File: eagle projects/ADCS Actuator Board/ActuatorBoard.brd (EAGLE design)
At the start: 91 x 91 mm, 278 parts, among them J19 TE_1-84953-1, J20 TE_1-84953-1, J21 TE_1-84953-1, U10 DRV10970_MOTOR_DRIVERDRV10970, U12 DRV10970_MOTOR_DRIVERDRV10970, U13 ADS7841E_2K5, U15 TLV9051IDCKR, U19 TLV9051IDCKR, U2 ADS7841E_2K5, U21 TLV9051IDCKR, U23 TLV9051IDCKR, U24 TLV9051IDCKR, U25 ADS7841E_2K5, U26 TLV9051IDCKR, U27 ADS7841E_2K5, U28 TLV9051IDCKR, U29 TLV9051IDCKR, U3 ADS7841E_2K5, U30 TLV9051IDCKR, U31 TLV9051IDCKR, U32 TLV9051IDCKR, U34 TVS991, U35 BD6210F-E2, U38 TVS991, U39 BD6210F-E2, U4 ADS7841E_2K5, U5 TVS991, U6 TLV9051IDCKR, U7 DRV10970_MOTOR_DRIVERDRV10970, U9 BD6210F-E2

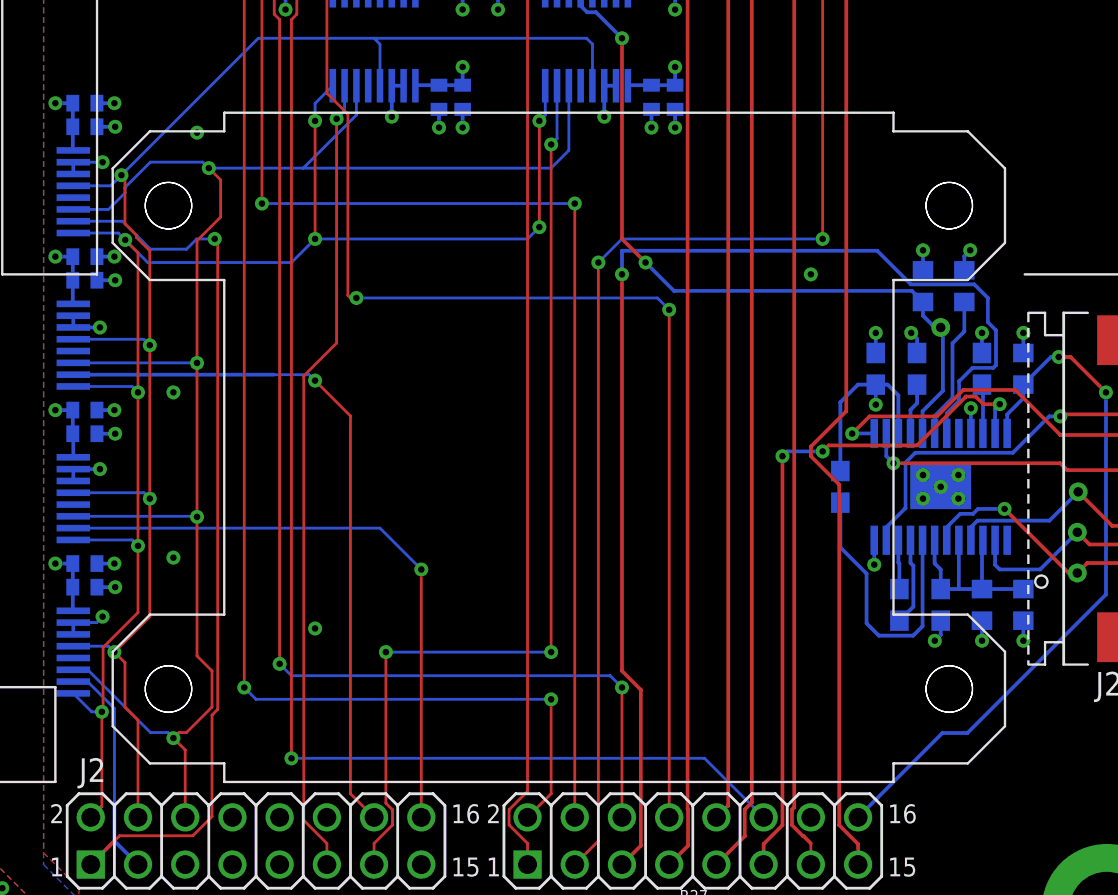
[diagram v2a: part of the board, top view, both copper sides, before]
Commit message: Updated new reaction wheel footprint, silk and 3d model
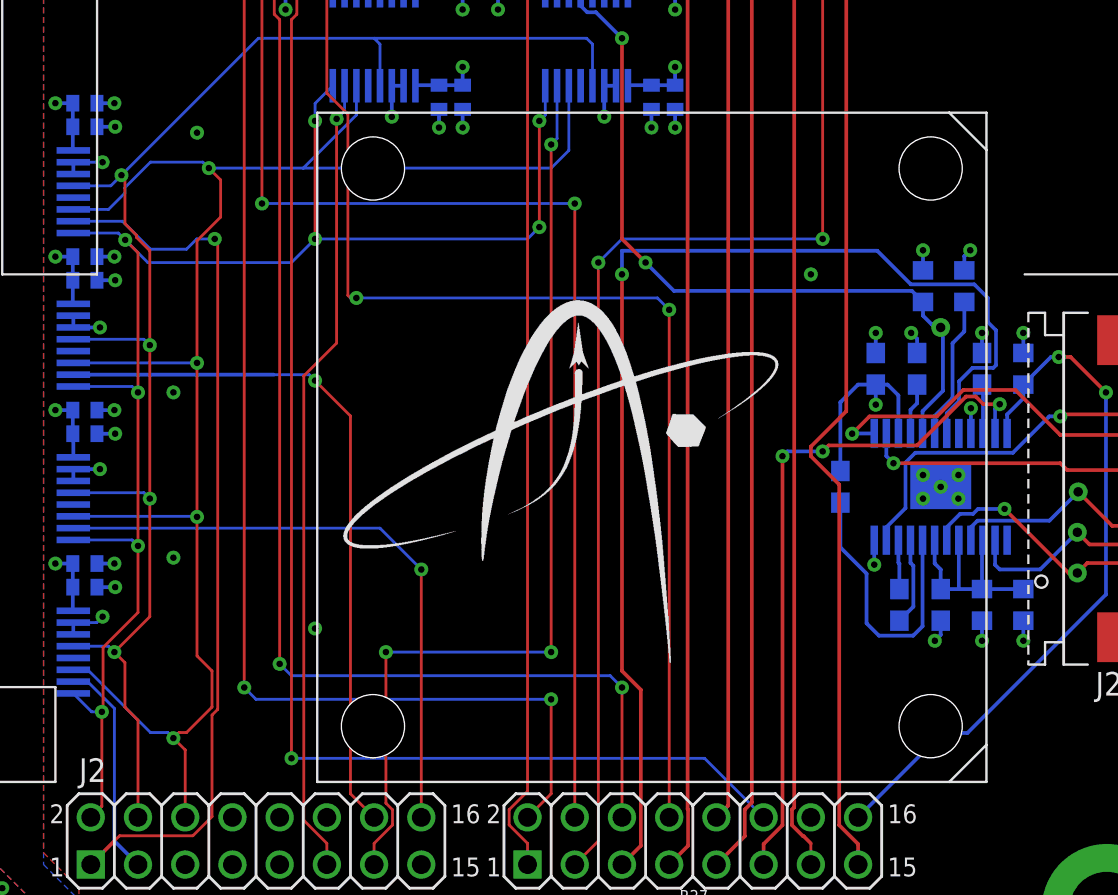
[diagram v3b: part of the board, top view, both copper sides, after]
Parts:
- moved RWZ 5.00 mm to (78.0, 13.3)

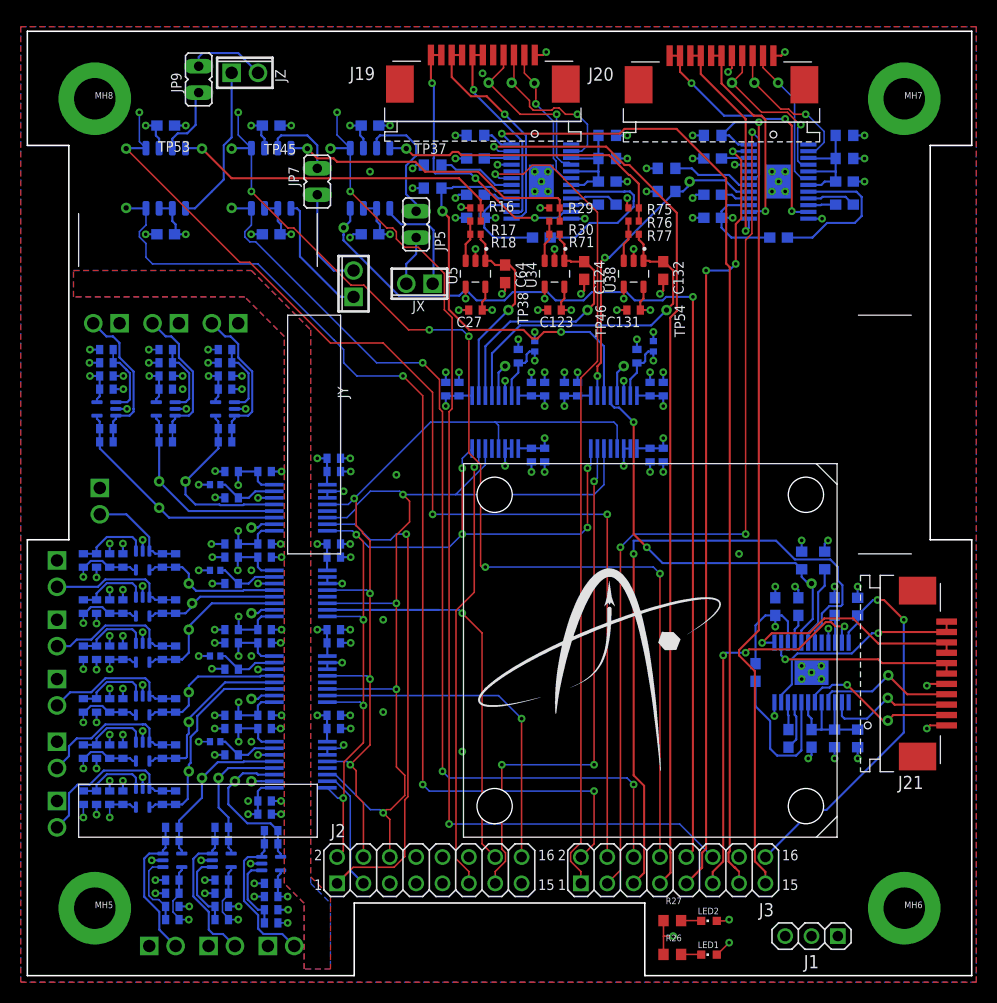
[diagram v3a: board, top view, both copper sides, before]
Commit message: Updates to layout silk/traces
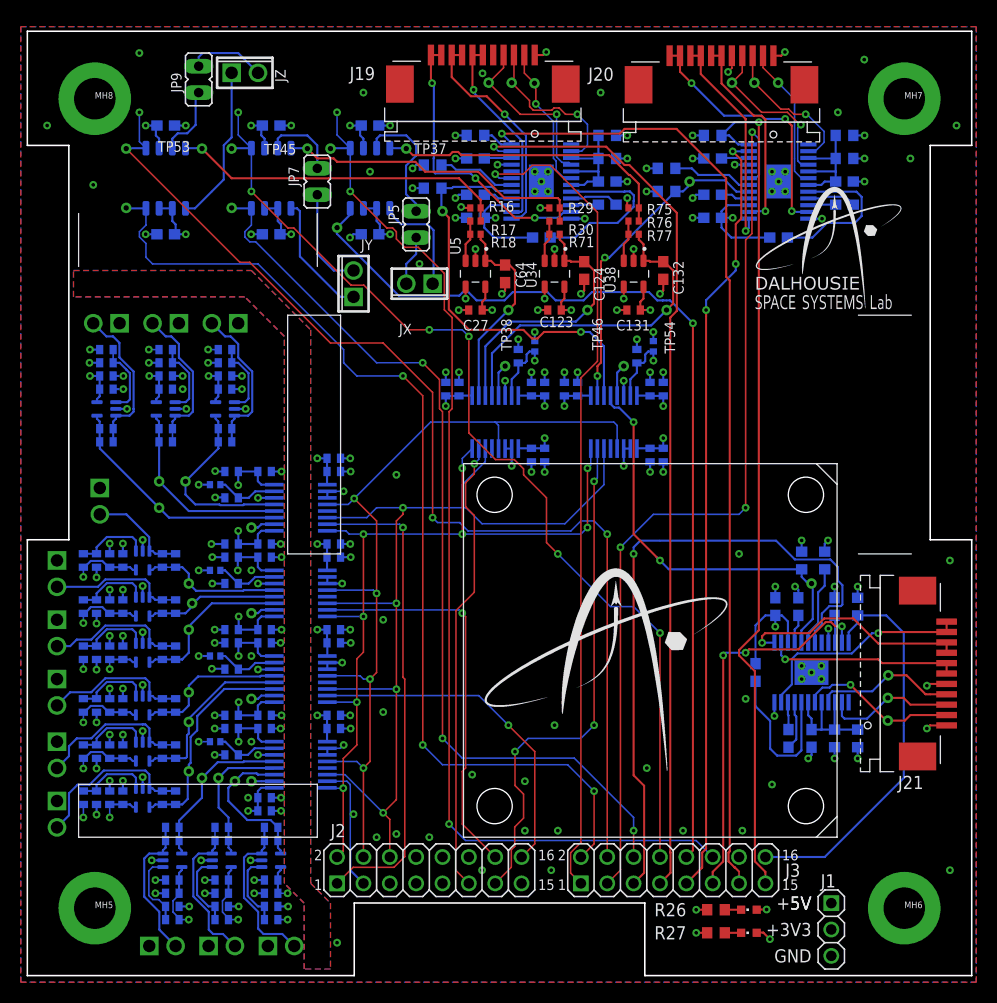
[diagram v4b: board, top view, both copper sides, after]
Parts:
- moved R26 6.02 mm to (66.4, 6.35)
- moved LED1 5.79 mm to (69.5, 6.35)
- moved R27 4.37 mm to (66.4, 4.13)
- moved LED2 4.01 mm to (69.5, 4.13)
- moved J1 2.01 mm to (77.5, 4.45), turned to 270 degrees
- moved TP35 0.64 mm to (29.8, 72.1)
- moved C91 0.32 mm to (22.9, 15.9)
- moved R62 0.32 mm to (23.5, 6.67)
- moved R64 0.32 mm to (23.5, 13.0)
- moved U30 0.32 mm to (23.5, 11.1)
- moved C96 0.32 mm to (23.5, 7.94)
- moved R63 0.32 mm to (23.5, 5.40)
- moved C92 0.32 mm to (22.9, 17.1)
- moved C97 0.32 mm to (23.5, 9.21)
- moved C98 0.32 mm to (23.5, 14.3)
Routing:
- net MAG_Y_RIN: track 104.3 -> 97.0 mm
- net MAG_Y_FIN: track 93.2 -> 89.5 mm
- net UCB0_SPI_CLK: track 84.5 -> 81.9 mm
- net MAG_Z_FIN: track 101.2 -> 99.0 mm
- net GND: track 170.7 -> 168.6 mm, vias 176 -> 177
- net !CS!_CUR_SENSE_RW: track 51.5 -> 49.6 mm
- net UCB0_SPI_MISO: track 83.6 -> 85.1 mm
- net RW_Y_SPEED_CTRL: track 90.0 -> 88.5 mm
- net RW_Y_DIR: track 75.9 -> 74.6 mm
- net MAG_X_FIN: track 95.4 -> 94.2 mm
- net RW_Z_I_SENS: track 40.3 -> 41.2 mm
- net UCB0_SPI_MOSI: track 95.1 -> 94.3 mm
- net +5V: track 66.4 -> 65.7 mm
- net !CS!_CUR_SENSE_MAG: track 43.3 -> 44.0 mm
- net !CS!_SUN_Y+: track 11.7 -> 12.4 mm
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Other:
- board text added: "+3V3"
- board text added: "+5V"
- board text added: "5V"
- board text added: "GND"

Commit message: Slight layout tweaks
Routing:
- net RW_Y_SPEED_CTRL: track 88.5 -> 82.5 mm
- net RW_Y_OUTFG: track 82.3 -> 77.4 mm
- net UCB0_SPI_CLK: track 81.9 -> 77.0 mm, vias 8 -> 7
- net Z_PHASE_B: track 22.4 -> 20.0 mm
- net MAG_Z_FIN: track 99.0 -> 101.2 mm
- net RW_Z_DIR: track 36.9 -> 38.0 mm
- net MAG_Z_RIN: track 106.4 -> 107.3 mm
- net Y_PHASE_B: track 21.0 -> 20.4 mm
- net !CS!_CUR_SENSE_RW: track 49.6 -> 49.1 mm

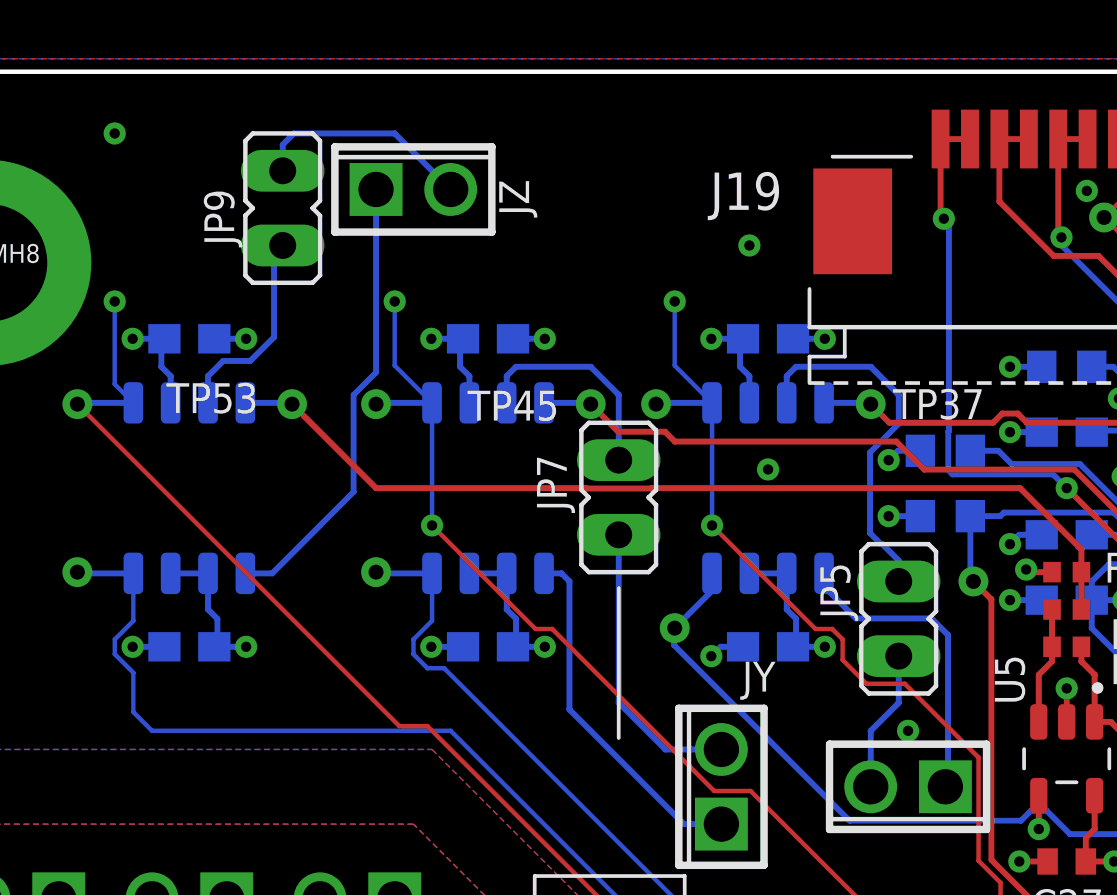
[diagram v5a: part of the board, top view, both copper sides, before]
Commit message: Replaced jumpers with circular pads
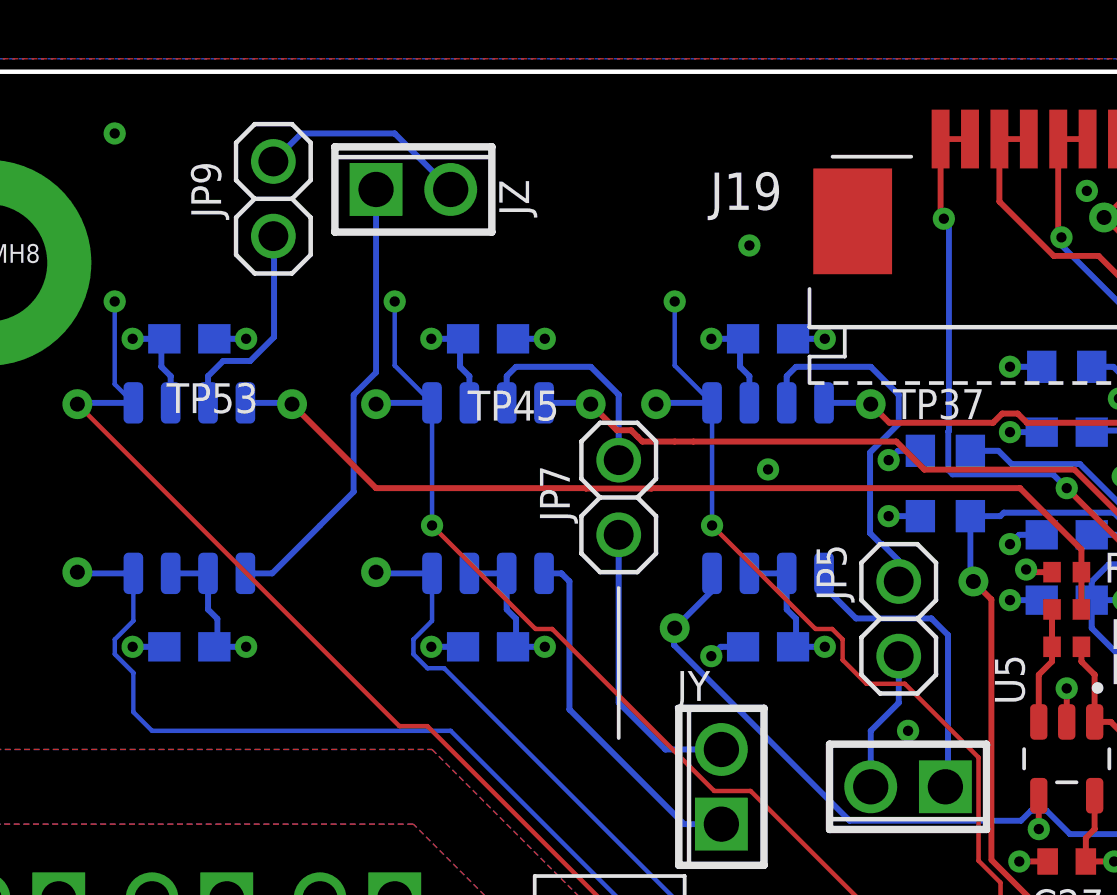
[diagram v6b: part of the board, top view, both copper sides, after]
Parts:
- JP5, JP7, JP9: device jumper:JP1 -> my_library:1X02
- moved JP9 0.45 mm to (16.2, 86.7), turned to 270 degrees
- turned JP5 to 90 degrees
- turned JP7 to 90 degrees
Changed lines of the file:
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@@
 <attribute name="SPICEPREFIX" value="C" x="33.02" y="61.9125" size="1.778" layer="28" rot="MR180" display="off"/>
 </element>
-<element name="JP5" library="jumper" library_urn="urn:adsk.eagle:library:252" package="JP1" package3d_urn="urn:adsk.eagle:package:15455/1" value="" x="37.465" y="72.39" smashed="yes">
-<attribute name="NAME" x="35.814" y="72.39" size="1.016" layer="25" ratio="10" rot="R90"/>
-<attribute name="POPULARITY" value="15" x="29.845" y="76.835" size="1.778" layer="27" display="off"/>
-<attribute name="VALUE" x="40.386" y="69.85" size="1.27" layer="27" ratio="10" rot="R90"/>
+<element name="JP5" library="my_library" library_urn="urn:adsk.eagle:library:22876504" package="1X02" package3d_urn="urn:adsk.eagle:package:24527019/1" value="" x="37.465" y="72.39" smashed="yes" rot="R90">
+<attribute name="NAME" x="34.671" y="74.93" size="1.016" layer="25" ratio="10" rot="R270"/>
+<attribute name="VALUE" x="40.005" y="75.311" size="1.27" layer="27" ratio="10" rot="R180"/>
 </element>
 <element name="C27" library="rcl" library_urn="urn:adsk.eagle:library:334" package="C0402" package3d_urn="urn:adsk.eagle:package:23626/2" value="0.1u" x="43.18" y="64.135" smashed="yes" rot="R180">
@@
 <attribute name="SPICEPREFIX" value="C" x="23.495" y="61.9125" size="1.778" layer="28" rot="MR180" display="off"/>
 </element>
-<element name="JP7" library="jumper" library_urn="urn:adsk.eagle:library:252" package="JP1" package3d_urn="urn:adsk.eagle:package:15455/1" value="" x="27.94" y="76.5175" smashed="yes">
-<attribute name="NAME" x="25.1587" y="77.978" size="1.016" layer="25" ratio="10" rot="R270"/>
-<attribute name="POPULARITY" value="15" x="20.32" y="80.9625" size="1.778" layer="27" display="off"/>
-<attribute name="VALUE" x="30.861" y="73.9775" size="1.27" layer="27" ratio="10" rot="R90"/>
+<element name="JP7" library="my_library" library_urn="urn:adsk.eagle:library:22876504" package="1X02" package3d_urn="urn:adsk.eagle:package:24527019/1" value="" x="27.94" y="76.5175" smashed="yes" rot="R90">
+<attribute name="NAME" x="26.2763" y="75.692" size="1.016" layer="25" ratio="10" rot="R90"/>
+<attribute name="VALUE" x="30.48" y="79.4385" size="1.27" layer="27" ratio="10" rot="R180"/>
 </element>
 <element name="C123" library="rcl" library_urn="urn:adsk.eagle:library:334" package="C0402" package3d_urn="urn:adsk.eagle:package:23626/2" value="0.1u" x="50.8" y="64.135" smashed="yes" rot="R180">
@@
 <attribute name="MF" value="" x="97.4725" y="41.275" size="1.778" layer="27" rot="R90" display="off"/>
 <attribute name="MPN" value="" x="97.4725" y="41.275" size="1.778" layer="27" rot="R90" display="off"/>
-<attribute name="NAME" x="33.274" y="70.9295" size="1.016" layer="25" rot="R180"/>
+<attribute name="NAME" x="31.0515" y="70.612" size="1.016" layer="25" rot="R180"/>
 <attribute name="OC_FARNELL" value="unknown" x="97.4725" y="41.275" size="1.778" layer="27" rot="R90" display="off"/>
 <attribute name="OC_NEWARK" value="unknown" x="97.4725" y="41.275" size="1.778" layer="27" rot="R90" display="off"/>
@@
 <attribute name="SPICEPREFIX" value="C" x="13.335" y="61.9125" size="1.778" layer="28" rot="MR180" display="off"/>
 </element>
-<element name="JP9" library="jumper" library_urn="urn:adsk.eagle:library:252" package="JP1" package3d_urn="urn:adsk.eagle:package:15455/1" value="" x="16.51" y="86.36" smashed="yes" rot="R180">
-<attribute name="NAME" x="14.859" y="85.09" size="1.016" layer="25" ratio="10" rot="R90"/>
-<attribute name="POPULARITY" value="15" x="24.13" y="81.915" size="1.778" layer="27" rot="R180" display="off"/>
-<attribute name="VALUE" x="13.589" y="88.9" size="1.27" layer="27" ratio="10" rot="R270"/>
+<element name="JP9" library="my_library" library_urn="urn:adsk.eagle:library:22876504" package="1X02" package3d_urn="urn:adsk.eagle:package:24527019/1" value="" x="16.1925" y="86.6775" smashed="yes" rot="R270">
+<attribute name="NAME" x="13.3985" y="87.9475" size="1.016" layer="25" ratio="10" rot="R270"/>
+<attribute name="VALUE" x="13.6525" y="83.7565" size="1.27" layer="27" ratio="10"/>
 </element>
 <element name="C131" library="rcl" library_urn="urn:adsk.eagle:library:334" package="C0402" package3d_urn="urn:adsk.eagle:package:23626/2" value="0.1u" x="58.42" y="64.135" smashed="yes" rot="R180">
@@
 <contactref element="JP9" pad="1"/>
 <contactref element="JZ" pad="2"/>
-<wire x1="22.225" y1="86.995" x2="20.32" y2="88.9" width="0.2032" layer="16"/>
-<wire x1="20.32" y1="88.9" x2="16.8907875" y2="88.9" width="0.2032" layer="16"/>
-<wire x1="16.8907875" y1="88.9" x2="16.51" y2="88.5192125" width="0.2032" layer="16"/>
-<wire x1="16.51" y1="88.5192125" x2="16.51" y2="87.63" width="0.2" layer="16"/>
+<wire x1="20.32" y1="88.9" x2="22.225" y2="86.995" width="0.2032" layer="16"/>
+<wire x1="16.1925" y1="87.9475" x2="17.145" y2="88.9" width="0.2032" layer="16"/>
+<wire x1="17.145" y1="88.9" x2="20.32" y2="88.9" width="0.2032" layer="16"/>
 </signal>
 <signal name="X_PHASE_C">
@@
 <contactref element="U39" pad="7"/>
 <wire x1="14.486" y1="81.161" x2="13.97" y2="80.645" width="0.2032" layer="16"/>
-<wire x1="16.51" y1="85.09" x2="16.2153" y2="84.7953" width="0.2032" layer="16"/>
+<wire x1="16.1925" y1="85.4075" x2="16.2153" y2="84.7953" width="0.2032" layer="16"/>
 <wire x1="16.2153" y1="84.7953" x2="16.2153" y2="81.97063125" width="0.2032" layer="16"/>
 <wire x1="16.2153" y1="81.97063125" x2="15.40566875" y2="81.161" width="0.2032" layer="16"/>
@@
 <wire x1="26.945" y1="79.735" x2="26.9875" y2="79.6925" width="0.2032" layer="16"/>
 <wire x1="51.3" y1="74.7475" x2="51.3" y2="73.9775" width="0.2032" layer="1"/>
-<wire x1="29.8478" y1="78.4197" x2="37.38376875" y2="78.4197" width="0.2032" layer="1"/>
+<wire x1="29.8478" y1="78.4197" x2="30.48" y2="78.4197" width="0.2032" layer="1"/>
+<wire x1="30.48" y1="78.4197" x2="37.38376875" y2="78.4197" width="0.2032" layer="1"/>
 <wire x1="51.3" y1="74.7475" x2="51.1147" y2="74.9328" width="0.2032" layer="1"/>
 <wire x1="51.1147" y1="74.9328" x2="46.3522" y2="74.9328" width="0.2032" layer="1"/>
 <wire x1="38.33346875" y1="77.47" x2="37.38376875" y2="78.4197" width="0.2032" layer="1"/>
-<wire x1="26.9875" y1="79.6925" x2="27.9273" y2="78.7527" width="0.2032" layer="1"/>
-<wire x1="27.9273" y1="78.7527" x2="29.5148" y2="78.7527" width="0.2032" layer="1"/>
-<wire x1="29.5148" y1="78.7527" x2="29.8478" y2="78.4197" width="0.2032" layer="1"/>
 <wire x1="46.3522" y1="74.9328" x2="45.97400625" y2="74.9328" width="0.2" layer="1"/>
 <wire x1="45.97400625" y1="74.9328" x2="43.44120625" y2="77.4656" width="0.2" layer="1"/>
 <wire x1="38.33786875" y1="77.4656" x2="38.33346875" y2="77.47" width="0.2" layer="1"/>
 <wire x1="43.44120625" y1="77.4656" x2="38.33786875" y2="77.4656" width="0.2" layer="1"/>
+<wire x1="27.8765" y1="78.8035" x2="26.9875" y2="79.6925" width="0.2032" layer="1"/>
+<wire x1="28.58309375" y1="78.58125" x2="28.36084375" y2="78.8035" width="0.2032" layer="1"/>
+<wire x1="28.36084375" y1="78.8035" x2="27.8765" y2="78.8035" width="0.2032" layer="1"/>
+<wire x1="28.58309375" y1="78.58125" x2="28.74464375" y2="78.4197" width="0.2032" layer="1"/>
+<wire x1="28.74464375" y1="78.4197" x2="29.8478" y2="78.4197" width="0.2032" layer="1"/>
 </signal>
 <signal name="N$62">

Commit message: solved drc errors
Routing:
- net UCB0_SPI_CLK: track 77.0 -> 81.9 mm, vias 7 -> 8
- net MAG_Y_FIN: track 89.5 -> 94.2 mm
